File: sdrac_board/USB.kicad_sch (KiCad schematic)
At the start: 8 parts, among them J6 USB_C_Receptacle_USB2.0, U10 USBLC6-2SC6

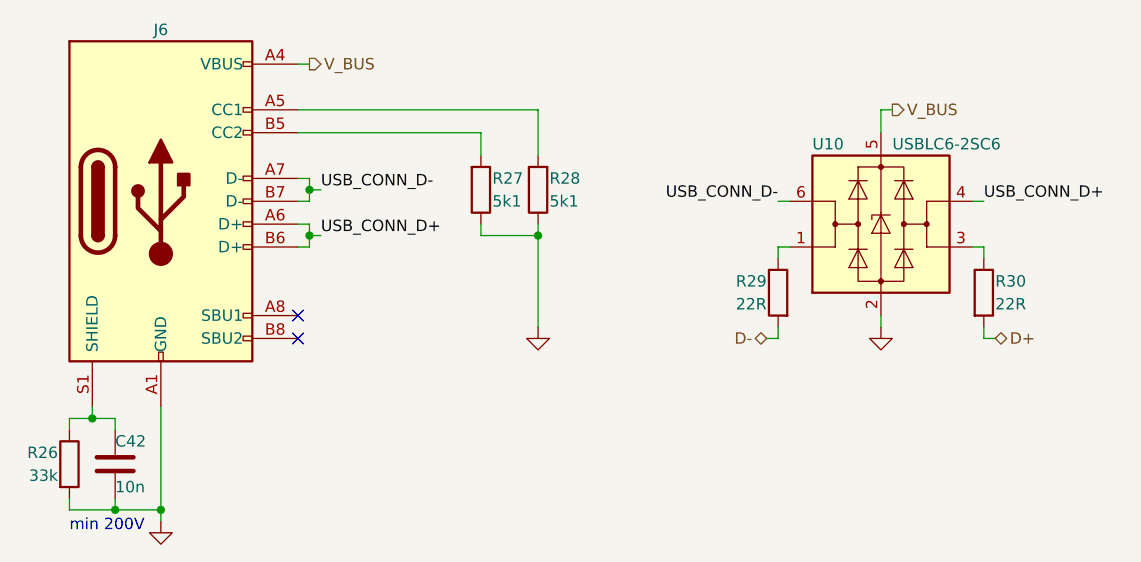
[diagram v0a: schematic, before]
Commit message: added second I2C communscation lane for synchronization and added wyas to change mcirosteping with resistors
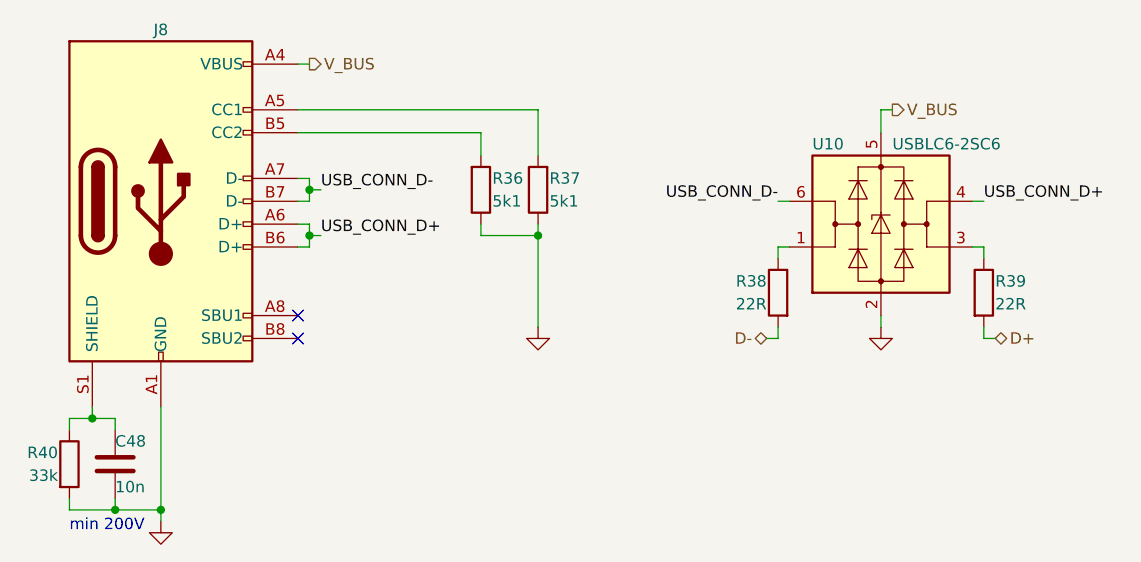
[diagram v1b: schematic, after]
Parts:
- renumbered C42 to C48, J6 to J8, R27 to R36, R28 to R37, R29 to R38, R30 to R39, R26 to R40
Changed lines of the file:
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@@
   (symbol (lib_id "power:GND") (at 111.76 129.54 0) (unit 1)
     (in_bom yes) (on_board yes) (dnp no)
-    (property "Reference" "#PWR067" (at 111.76 135.89 0)
+    (property "Reference" "#PWR086" (at 111.76 135.89 0)
       (effects (font (size 1.27 1.27)) hide)
     )
@@
       (project "sdrac_board"
         (path "/7e6d1db5-12f1-49d6-b3bd-d624ec5345e8/817b1694-e153-40b5-9fd9-c7030af4d887"
-          (reference "#PWR067") (unit 1)
+          (reference "#PWR086") (unit 1)
         )
       )
@@
   (symbol (lib_id "power:GND") (at 191.77 107.95 0) (unit 1)
     (in_bom yes) (on_board yes) (dnp no)
-    (property "Reference" "#PWR069" (at 191.77 114.3 0)
+    (property "Reference" "#PWR085" (at 191.77 114.3 0)
       (effects (font (size 1.27 1.27)) hide)
     )
@@
       (project "sdrac_board"
         (path "/7e6d1db5-12f1-49d6-b3bd-d624ec5345e8/817b1694-e153-40b5-9fd9-c7030af4d887"
-          (reference "#PWR069") (unit 1)
+          (reference "#PWR085") (unit 1)
         )
       )
@@
   (symbol (lib_id "Device:C") (at 106.68 123.19 0) (unit 1)
     (in_bom yes) (on_board yes) (dnp no)
-    (property "Reference" "C42" (at 106.68 120.65 0)
+    (property "Reference" "C48" (at 106.68 120.65 0)
       (effects (font (size 1.27 1.27)) (justify left))
     )
@@
       (project "sdrac_board"
         (path "/7e6d1db5-12f1-49d6-b3bd-d624ec5345e8/817b1694-e153-40b5-9fd9-c7030af4d887"
-          (reference "C42") (unit 1)
+          (reference "C48") (unit 1)
         )
       )
@@
   (symbol (lib_id "Device:R") (at 153.67 92.71 180) (unit 1)
     (in_bom yes) (on_board yes) (dnp no)
-    (property "Reference" "R28" (at 154.94 91.44 0)
+    (property "Reference" "R37" (at 154.94 91.44 0)
       (effects (font (size 1.27 1.27)) (justify right))
     )
@@
       (project "sdrac_board"
         (path "/7e6d1db5-12f1-49d6-b3bd-d624ec5345e8/817b1694-e153-40b5-9fd9-c7030af4d887"
-          (reference "R28") (unit 1)
+          (reference "R37") (unit 1)
         )
       )
@@
   (symbol (lib_id "Connector:USB_C_Receptacle_USB2.0") (at 111.76 93.98 0) (unit 1)
     (in_bom yes) (on_board yes) (dnp no)
-    (property "Reference" "J6" (at 111.76 74.93 0)
+    (property "Reference" "J8" (at 111.76 74.93 0)
       (effects (font (size 1.27 1.27)))
     )
@@
       (project "sdrac_board"
         (path "/7e6d1db5-12f1-49d6-b3bd-d624ec5345e8/817b1694-e153-40b5-9fd9-c7030af4d887"
+          (reference "J8") (unit 1)
+        )
+      )
+      (project "motor controller"
+        (path "/98359aeb-e3f0-4579-a083-8ca5fb10d8d7/bc95d4f1-94c9-4f57-b21a-236195f7bb70"
           (reference "J6") (unit 1)
         )
       )
-      (project "motor controller"
-        (path "/98359aeb-e3f0-4579-a083-8ca5fb10d8d7/bc95d4f1-94c9-4f57-b21a-236195f7bb70"
-          (reference "J6") (unit 1)
-        )
-      )
     )
   )
   (symbol (lib_id "Device:R") (at 147.32 92.71 0) (mirror x) (unit 1)
     (in_bom yes) (on_board yes) (dnp no)
-    (property "Reference" "R27" (at 148.59 91.44 0)
+    (property "Reference" "R36" (at 148.59 91.44 0)
       (effects (font (size 1.27 1.27)) (justify left))
     )
@@
       (project "sdrac_board"
         (path "/7e6d1db5-12f1-49d6-b3bd-d624ec5345e8/817b1694-e153-40b5-9fd9-c7030af4d887"
-          (reference "R27") (unit 1)
+          (reference "R36") (unit 1)
         )
       )
@@
   (symbol (lib_id "Device:R") (at 180.34 104.14 0) (mirror y) (unit 1)
     (in_bom yes) (on_board yes) (dnp no)
-    (property "Reference" "R29" (at 179.07 102.87 0)
+    (property "Reference" "R38" (at 179.07 102.87 0)
       (effects (font (size 1.27 1.27)) (justify left))
     )
@@
       (project "sdrac_board"
         (path "/7e6d1db5-12f1-49d6-b3bd-d624ec5345e8/817b1694-e153-40b5-9fd9-c7030af4d887"
-          (reference "R29") (unit 1)
+          (reference "R38") (unit 1)
         )
       )
@@
   (symbol (lib_id "Device:R") (at 203.2 104.14 0) (unit 1)
     (in_bom yes) (on_board yes) (dnp no)
-    (property "Reference" "R30" (at 204.47 102.87 0)
+    (property "Reference" "R39" (at 204.47 102.87 0)
       (effects (font (size 1.27 1.27)) (justify left))
     )
@@
       (project "sdrac_board"
         (path "/7e6d1db5-12f1-49d6-b3bd-d624ec5345e8/817b1694-e153-40b5-9fd9-c7030af4d887"
-          (reference "R30") (unit 1)
+          (reference "R39") (unit 1)
         )
       )
@@
   (symbol (lib_id "power:GND") (at 153.67 107.95 0) (unit 1)
     (in_bom yes) (on_board yes) (dnp no)
-    (property "Reference" "#PWR068" (at 153.67 114.3 0)
+    (property "Reference" "#PWR084" (at 153.67 114.3 0)
       (effects (font (size 1.27 1.27)) hide)
     )
@@
       (project "sdrac_board"
         (path "/7e6d1db5-12f1-49d6-b3bd-d624ec5345e8/817b1694-e153-40b5-9fd9-c7030af4d887"
-          (reference "#PWR068") (unit 1)
+          (reference "#PWR084") (unit 1)
         )
       )
@@
   (symbol (lib_id "Device:R") (at 101.6 123.19 0) (unit 1)
     (in_bom yes) (on_board yes) (dnp no)
-    (property "Reference" "R26" (at 100.33 121.92 0)
+    (property "Reference" "R40" (at 100.33 121.92 0)
       (effects (font (size 1.27 1.27)) (justify right))
     )
@@
       (project "sdrac_board"
         (path "/7e6d1db5-12f1-49d6-b3bd-d624ec5345e8/817b1694-e153-40b5-9fd9-c7030af4d887"
-          (reference "R26") (unit 1)
-        )
-      )
+          (reference "R40") (unit 1)
+        )
+      )

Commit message: added hardware address selector
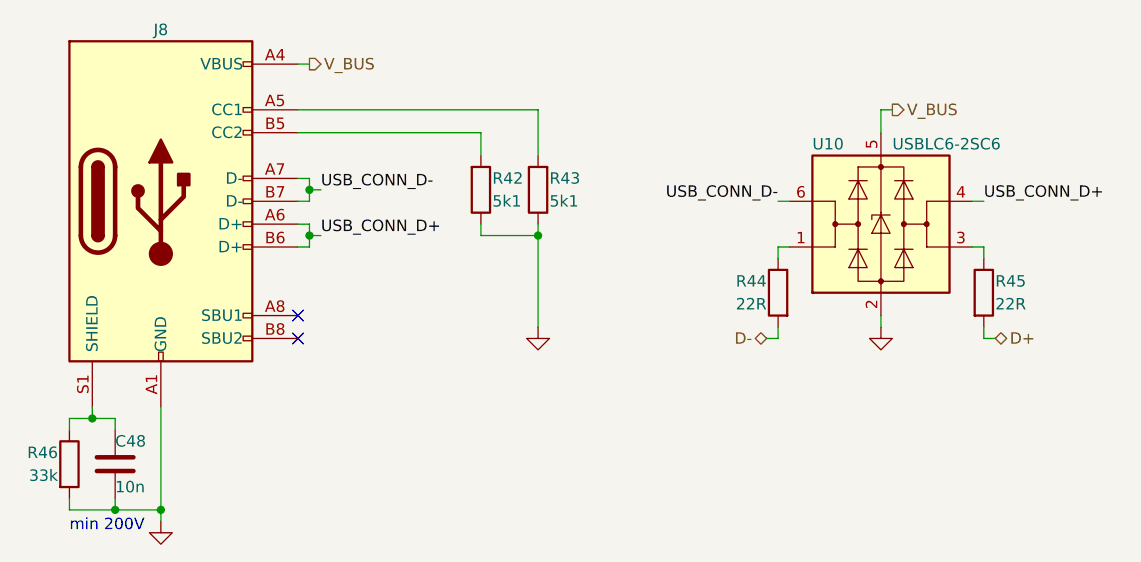
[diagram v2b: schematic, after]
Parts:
- renumbered R36 to R42, R37 to R43, R38 to R44, R39 to R45, R40 to R46
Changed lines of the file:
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@@
   (symbol (lib_id "power:GND") (at 111.76 129.54 0) (unit 1)
     (in_bom yes) (on_board yes) (dnp no)
-    (property "Reference" "#PWR086" (at 111.76 135.89 0)
+    (property "Reference" "#PWR092" (at 111.76 135.89 0)
       (effects (font (size 1.27 1.27)) hide)
     )
@@
       (project "sdrac_board"
         (path "/7e6d1db5-12f1-49d6-b3bd-d624ec5345e8/817b1694-e153-40b5-9fd9-c7030af4d887"
-          (reference "#PWR086") (unit 1)
+          (reference "#PWR092") (unit 1)
         )
       )
@@
   (symbol (lib_id "power:GND") (at 191.77 107.95 0) (unit 1)
     (in_bom yes) (on_board yes) (dnp no)
-    (property "Reference" "#PWR085" (at 191.77 114.3 0)
+    (property "Reference" "#PWR091" (at 191.77 114.3 0)
       (effects (font (size 1.27 1.27)) hide)
     )
@@
       (project "sdrac_board"
         (path "/7e6d1db5-12f1-49d6-b3bd-d624ec5345e8/817b1694-e153-40b5-9fd9-c7030af4d887"
-          (reference "#PWR085") (unit 1)
+          (reference "#PWR091") (unit 1)
         )
       )
@@
   (symbol (lib_id "Device:R") (at 153.67 92.71 180) (unit 1)
     (in_bom yes) (on_board yes) (dnp no)
-    (property "Reference" "R37" (at 154.94 91.44 0)
+    (property "Reference" "R43" (at 154.94 91.44 0)
       (effects (font (size 1.27 1.27)) (justify right))
     )
@@
       (project "sdrac_board"
         (path "/7e6d1db5-12f1-49d6-b3bd-d624ec5345e8/817b1694-e153-40b5-9fd9-c7030af4d887"
-          (reference "R37") (unit 1)
+          (reference "R43") (unit 1)
         )
       )
@@
   (symbol (lib_id "Device:R") (at 147.32 92.71 0) (mirror x) (unit 1)
     (in_bom yes) (on_board yes) (dnp no)
-    (property "Reference" "R36" (at 148.59 91.44 0)
+    (property "Reference" "R42" (at 148.59 91.44 0)
       (effects (font (size 1.27 1.27)) (justify left))
     )
@@
       (project "sdrac_board"
         (path "/7e6d1db5-12f1-49d6-b3bd-d624ec5345e8/817b1694-e153-40b5-9fd9-c7030af4d887"
-          (reference "R36") (unit 1)
+          (reference "R42") (unit 1)
         )
       )
@@
   (symbol (lib_id "Device:R") (at 180.34 104.14 0) (mirror y) (unit 1)
     (in_bom yes) (on_board yes) (dnp no)
-    (property "Reference" "R38" (at 179.07 102.87 0)
+    (property "Reference" "R44" (at 179.07 102.87 0)
       (effects (font (size 1.27 1.27)) (justify left))
     )
@@
       (project "sdrac_board"
         (path "/7e6d1db5-12f1-49d6-b3bd-d624ec5345e8/817b1694-e153-40b5-9fd9-c7030af4d887"
-          (reference "R38") (unit 1)
+          (reference "R44") (unit 1)
         )
       )
@@
   (symbol (lib_id "Device:R") (at 203.2 104.14 0) (unit 1)
     (in_bom yes) (on_board yes) (dnp no)
-    (property "Reference" "R39" (at 204.47 102.87 0)
+    (property "Reference" "R45" (at 204.47 102.87 0)
       (effects (font (size 1.27 1.27)) (justify left))
     )
@@
       (project "sdrac_board"
         (path "/7e6d1db5-12f1-49d6-b3bd-d624ec5345e8/817b1694-e153-40b5-9fd9-c7030af4d887"
-          (reference "R39") (unit 1)
+          (reference "R45") (unit 1)
         )
       )
@@
   (symbol (lib_id "power:GND") (at 153.67 107.95 0) (unit 1)
     (in_bom yes) (on_board yes) (dnp no)
-    (property "Reference" "#PWR084" (at 153.67 114.3 0)
+    (property "Reference" "#PWR090" (at 153.67 114.3 0)
       (effects (font (size 1.27 1.27)) hide)
     )
@@
       (project "sdrac_board"
         (path "/7e6d1db5-12f1-49d6-b3bd-d624ec5345e8/817b1694-e153-40b5-9fd9-c7030af4d887"
-          (reference "#PWR084") (unit 1)
+          (reference "#PWR090") (unit 1)
         )
       )
@@
   (symbol (lib_id "Device:R") (at 101.6 123.19 0) (unit 1)
     (in_bom yes) (on_board yes) (dnp no)
-    (property "Reference" "R40" (at 100.33 121.92 0)
+    (property "Reference" "R46" (at 100.33 121.92 0)
       (effects (font (size 1.27 1.27)) (justify right))
     )
@@
       (project "sdrac_board"
         (path "/7e6d1db5-12f1-49d6-b3bd-d624ec5345e8/817b1694-e153-40b5-9fd9-c7030af4d887"
-          (reference "R40") (unit 1)
-        )
-      )
+          (reference "R46") (unit 1)
+        )
+      )

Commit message: added 10A screw terminal
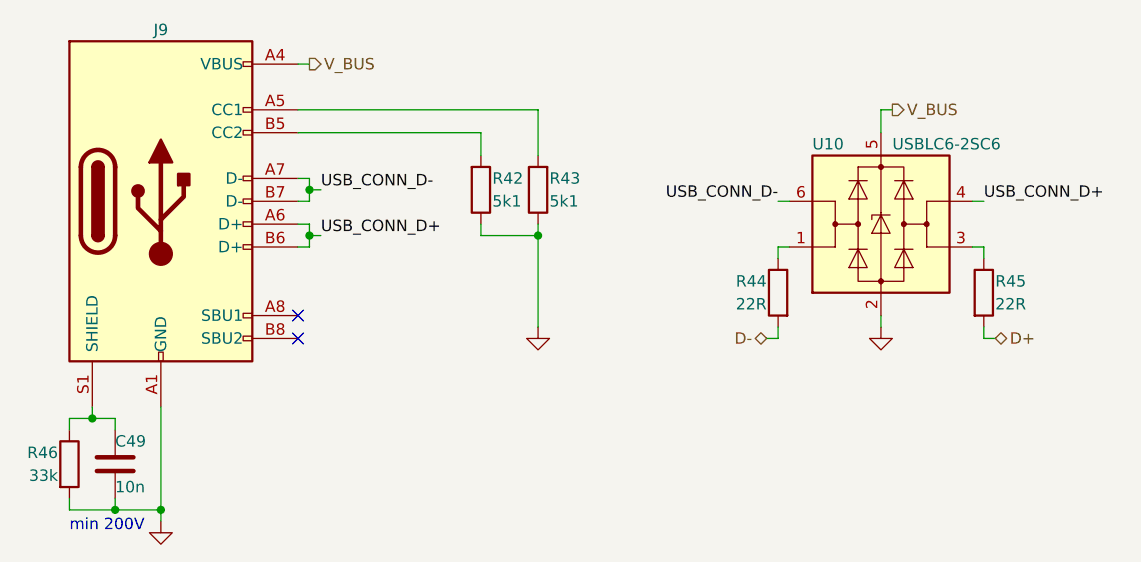
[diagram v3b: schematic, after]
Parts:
- renumbered C48 to C49, J8 to J9
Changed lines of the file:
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@@
   (symbol (lib_id "power:GND") (at 111.76 129.54 0) (unit 1)
     (in_bom yes) (on_board yes) (dnp no)
-    (property "Reference" "#PWR092" (at 111.76 135.89 0)
+    (property "Reference" "#PWR094" (at 111.76 135.89 0)
       (effects (font (size 1.27 1.27)) hide)
     )
@@
       (project "sdrac_board"
         (path "/7e6d1db5-12f1-49d6-b3bd-d624ec5345e8/817b1694-e153-40b5-9fd9-c7030af4d887"
-          (reference "#PWR092") (unit 1)
+          (reference "#PWR094") (unit 1)
         )
       )
@@
   (symbol (lib_id "power:GND") (at 191.77 107.95 0) (unit 1)
     (in_bom yes) (on_board yes) (dnp no)
-    (property "Reference" "#PWR091" (at 191.77 114.3 0)
+    (property "Reference" "#PWR093" (at 191.77 114.3 0)
       (effects (font (size 1.27 1.27)) hide)
     )
@@
       (project "sdrac_board"
         (path "/7e6d1db5-12f1-49d6-b3bd-d624ec5345e8/817b1694-e153-40b5-9fd9-c7030af4d887"
-          (reference "#PWR091") (unit 1)
+          (reference "#PWR093") (unit 1)
         )
       )
@@
   (symbol (lib_id "Device:C") (at 106.68 123.19 0) (unit 1)
     (in_bom yes) (on_board yes) (dnp no)
-    (property "Reference" "C48" (at 106.68 120.65 0)
+    (property "Reference" "C49" (at 106.68 120.65 0)
       (effects (font (size 1.27 1.27)) (justify left))
     )
@@
       (project "sdrac_board"
         (path "/7e6d1db5-12f1-49d6-b3bd-d624ec5345e8/817b1694-e153-40b5-9fd9-c7030af4d887"
-          (reference "C48") (unit 1)
+          (reference "C49") (unit 1)
         )
       )
@@
   (symbol (lib_id "Connector:USB_C_Receptacle_USB2.0") (at 111.76 93.98 0) (unit 1)
     (in_bom yes) (on_board yes) (dnp no)
-    (property "Reference" "J8" (at 111.76 74.93 0)
+    (property "Reference" "J9" (at 111.76 74.93 0)
       (effects (font (size 1.27 1.27)))
     )
@@
       (project "sdrac_board"
         (path "/7e6d1db5-12f1-49d6-b3bd-d624ec5345e8/817b1694-e153-40b5-9fd9-c7030af4d887"
-          (reference "J8") (unit 1)
+          (reference "J9") (unit 1)
         )
       )
@@
   (symbol (lib_id "power:GND") (at 153.67 107.95 0) (unit 1)
     (in_bom yes) (on_board yes) (dnp no)
-    (property "Reference" "#PWR090" (at 153.67 114.3 0)
+    (property "Reference" "#PWR092" (at 153.67 114.3 0)
       (effects (font (size 1.27 1.27)) hide)
     )
@@
       (project "sdrac_board"
         (path "/7e6d1db5-12f1-49d6-b3bd-d624ec5345e8/817b1694-e153-40b5-9fd9-c7030af4d887"
-          (reference "#PWR090") (unit 1)
-        )
-      )
+          (reference "#PWR092") (unit 1)
+        )
+      )

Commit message: fixwed resistors values
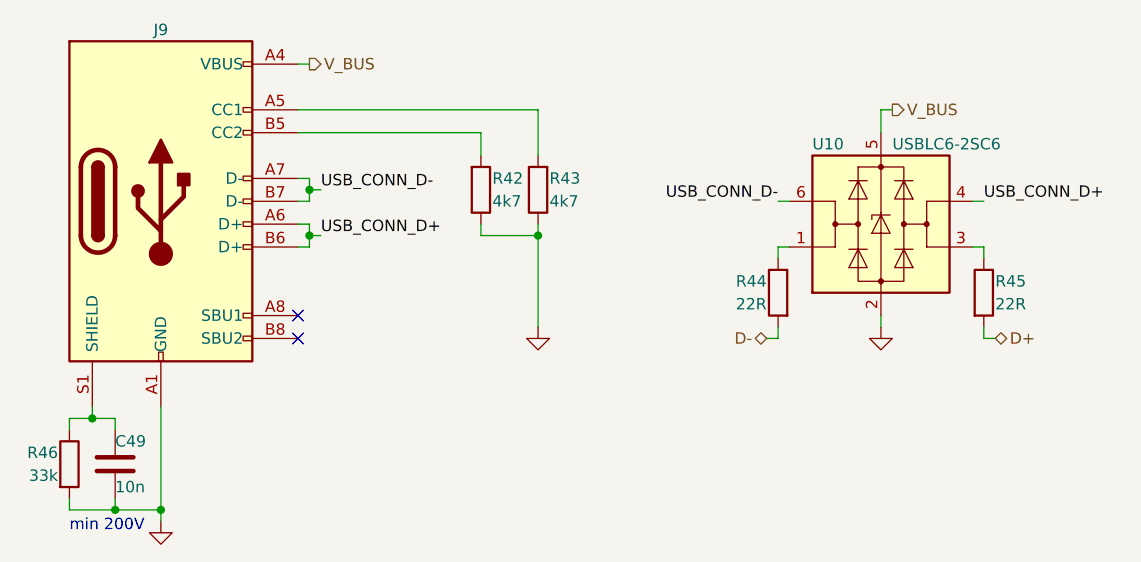
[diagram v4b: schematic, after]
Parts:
- R42, R43: value 5k1 -> 4k7
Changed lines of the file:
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@@
       (effects (font (size 1.27 1.27)) (justify right))
     )
-    (property "Value" "5k1" (at 154.94 93.98 0)
+    (property "Value" "4k7" (at 154.94 93.98 0)
       (effects (font (size 1.27 1.27)) (justify right))
     )
@@
       (effects (font (size 1.27 1.27)) (justify left))
     )
-    (property "Value" "5k1" (at 148.59 93.98 0)
+    (property "Value" "4k7" (at 148.59 93.98 0)
       (effects (font (size 1.27 1.27)) (justify left))
     )
